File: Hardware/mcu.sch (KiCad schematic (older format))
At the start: 0 parts

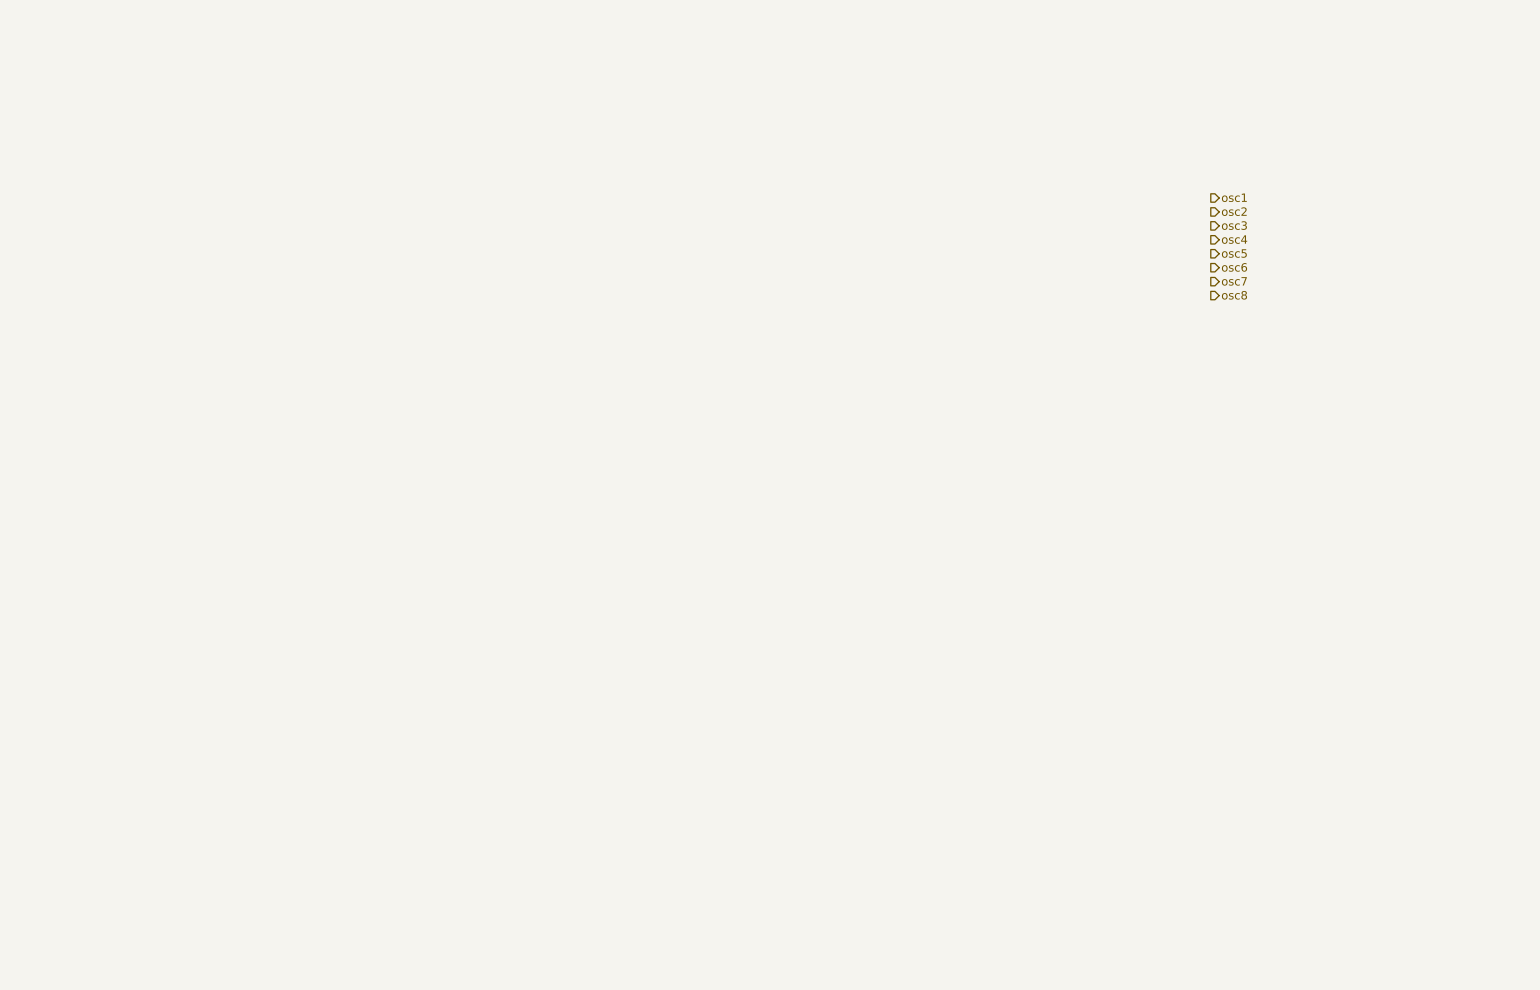
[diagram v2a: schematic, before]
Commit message: add all potentiometers for freq and pulse width
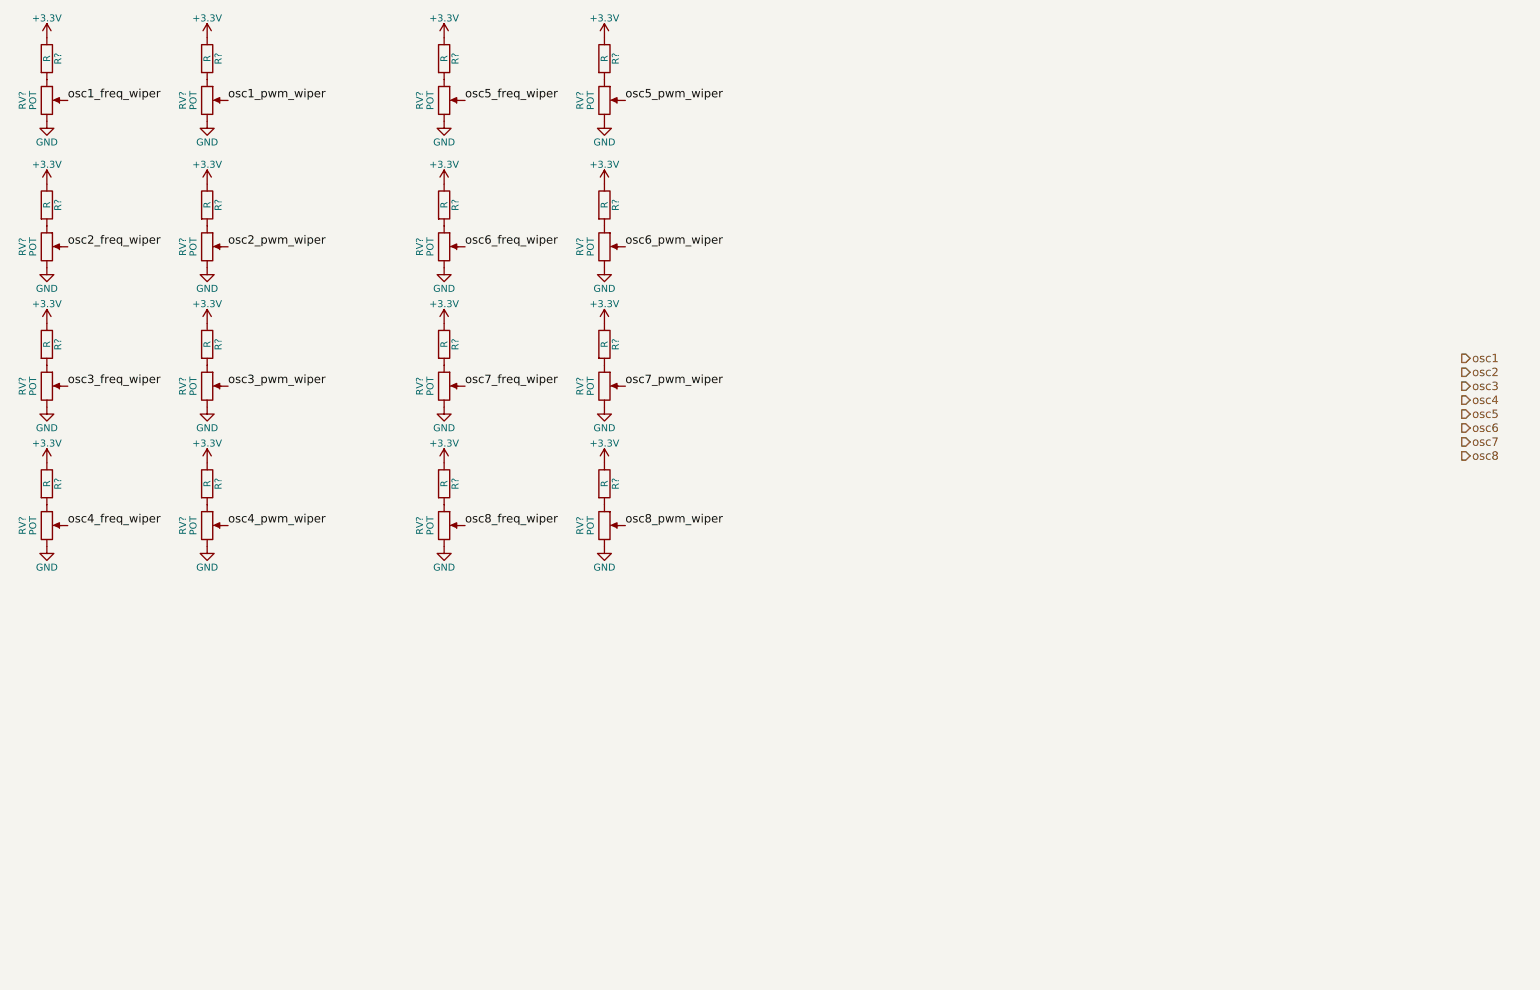
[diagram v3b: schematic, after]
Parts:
- added R? (x16): R, symbol R
- added RV? (x16): POT, symbol POT
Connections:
- new net: R?.2, RV?.1 (x16)
- new net +3V3: R?.1, R?.1, R?.1, R?.1, R?.1, R?.1, R?.1, R?.1, R?.1, R?.1, R?.1, R?.1, R?.1, R?.1, R?.1, R?.1
- new net GND: RV?.3, RV?.3, RV?.3, RV?.3, RV?.3, RV?.3, RV?.3, RV?.3, RV?.3, RV?.3, RV?.3, RV?.3, RV?.3, RV?.3, RV?.3, RV?.3
- new net osc1_freq_wiper: RV?.2
- new net osc1_pwm_wiper: RV?.2
- new net osc2_freq_wiper: RV?.2
- new net osc2_pwm_wiper: RV?.2
- new net osc3_freq_wiper: RV?.2
- new net osc3_pwm_wiper: RV?.2
- new net osc4_freq_wiper: RV?.2
- new net osc4_pwm_wiper: RV?.2
- new net osc5_freq_wiper: RV?.2
- new net osc5_pwm_wiper: RV?.2
- new net osc6_freq_wiper: RV?.2
- new net osc6_pwm_wiper: RV?.2
- new net osc7_freq_wiper: RV?.2
- new net osc7_pwm_wiper: RV?.2
- new net osc8_freq_wiper: RV?.2
- new net osc8_pwm_wiper: RV?.2

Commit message: add mcu, crystal, and programming header to schematic
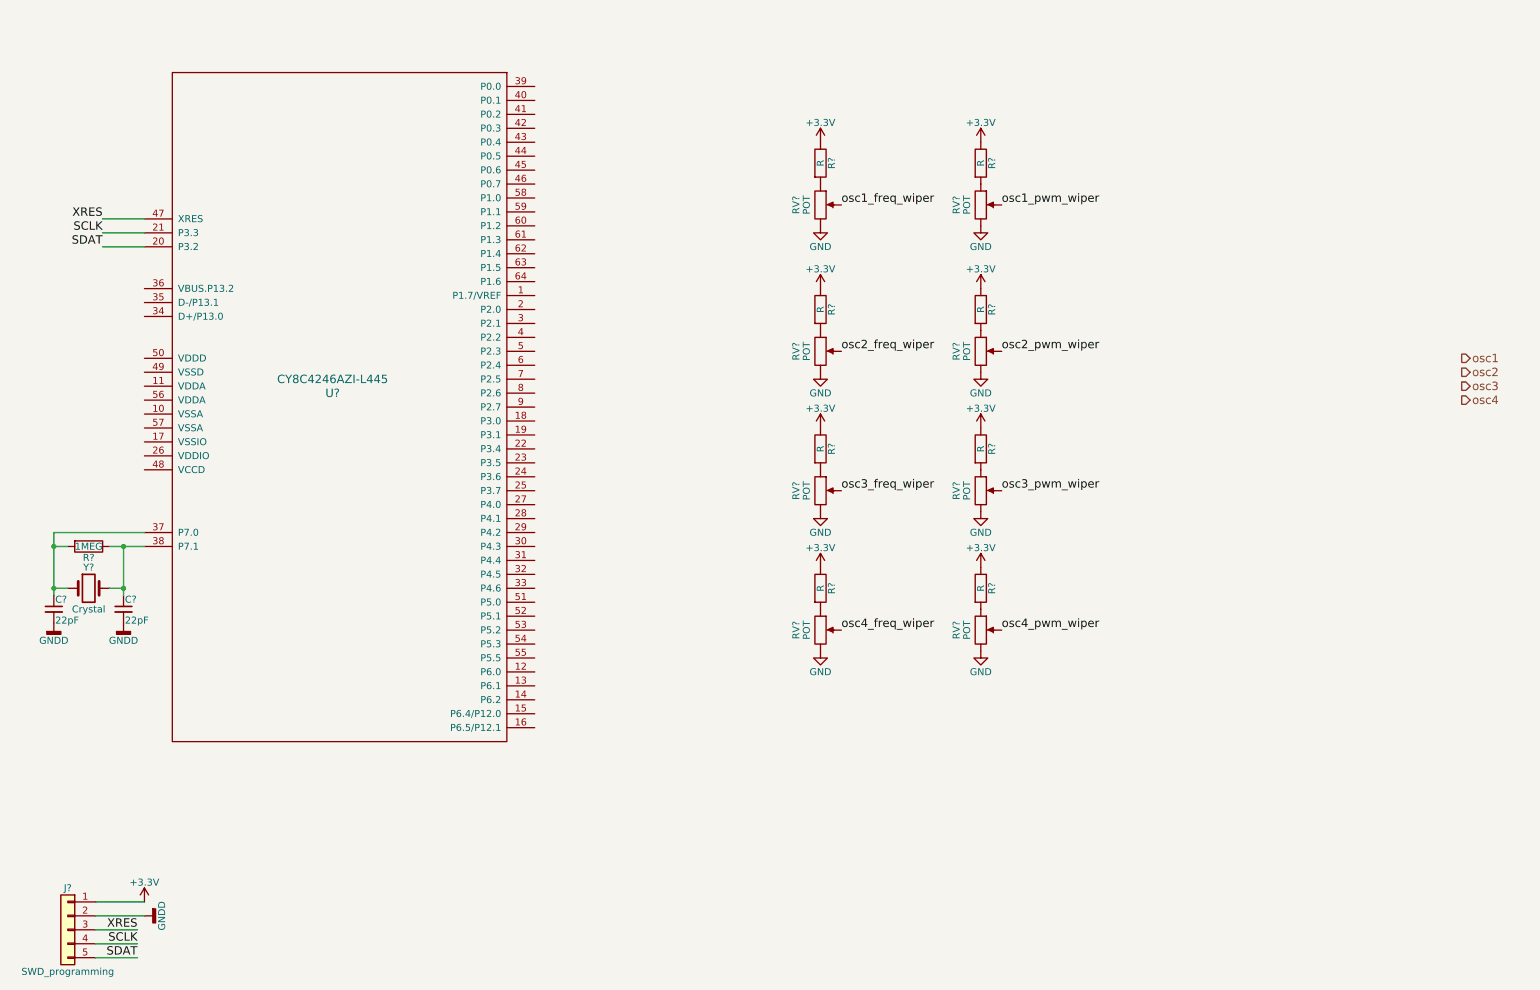
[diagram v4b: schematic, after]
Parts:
- removed R? (x8): R, symbol R
- removed RV? (x8): POT, symbol POT
- added C? (x2): 22pF, symbol C_Small
- added J?: SWD_programming, symbol Conn_01x05
- added R?: 1MEG, symbol R
- added U?: CY8C4246AZI-L445, symbol CY8C4246AZI-L445
- added Y?: Crystal, symbol Crystal
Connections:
- net +3V3: now also J?.1 (Pin_1)
- new net: C?.1, R?.2, U?.37 (P7.0), Y?.1
- new net: C?.1, R?.1, U?.38 (P7.1), Y?.2
- new net GNDD: C?.2, C?.2, J?.2 (Pin_2)
- new net SCLK: J?.4 (Pin_4), U?.21 (P3.3)
- new net SDAT: J?.5 (Pin_5), U?.20 (P3.2)
- new net XRES: J?.3 (Pin_3), U?.47 (XRES)
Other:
- moved on the sheet: R?, RV?

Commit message: connect frequency potentiometers to mcu
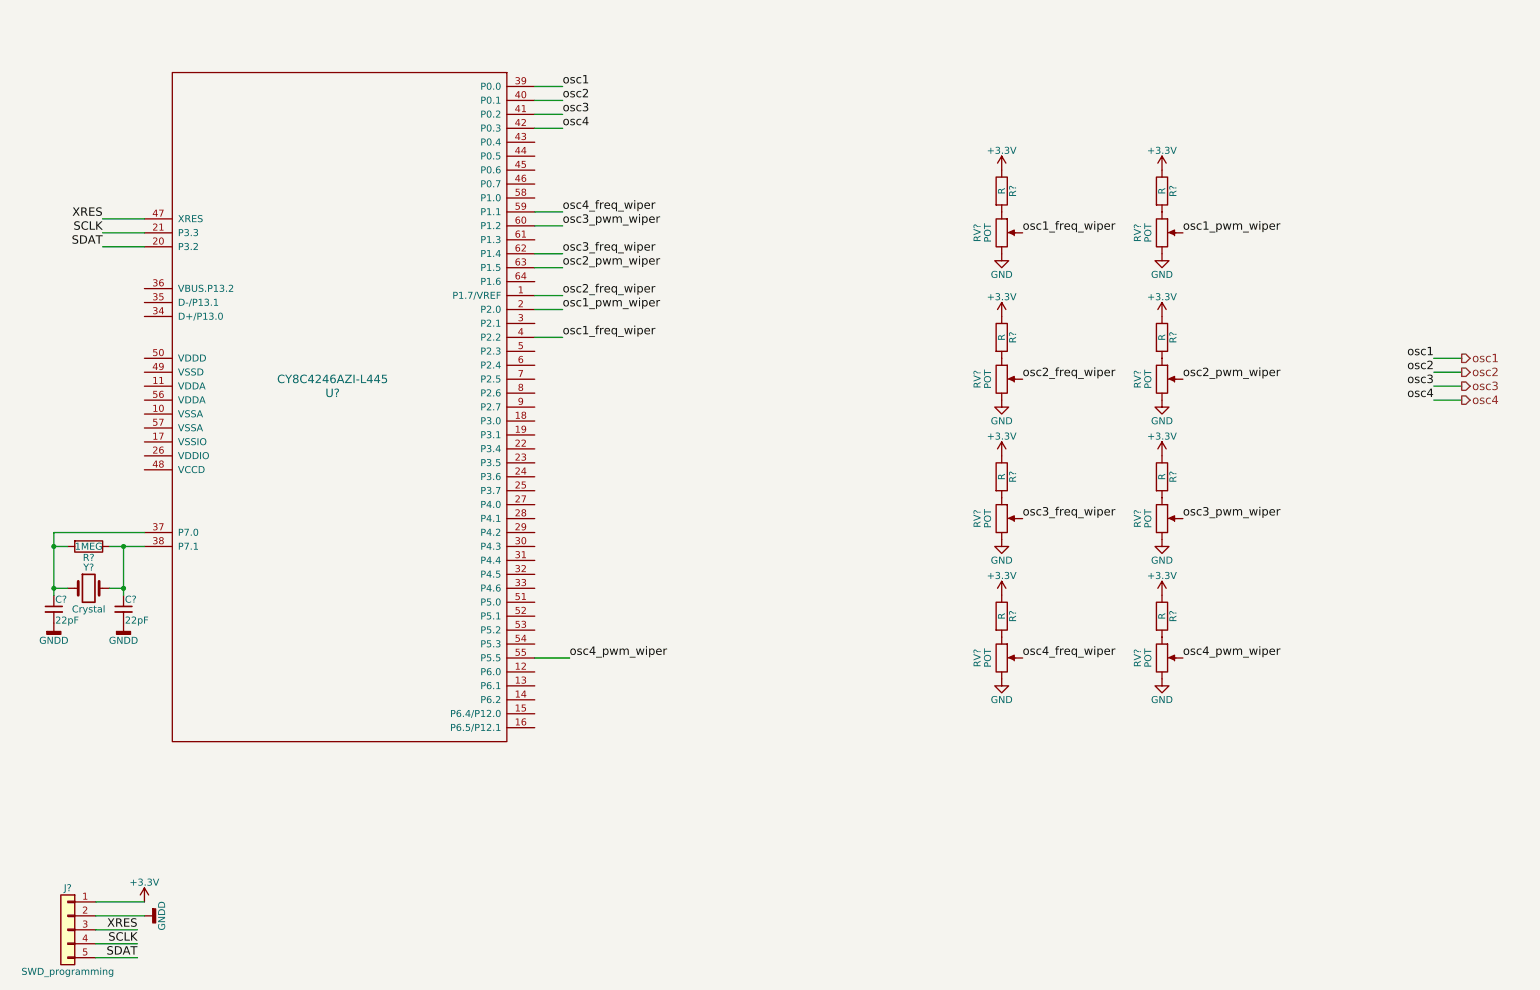
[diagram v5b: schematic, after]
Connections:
- net osc1: now also U?.39 (P0.0)
- net osc1_freq_wiper: now also U?.4 (P2.2)
- net osc1_pwm_wiper: now also U?.2 (P2.0)
- net osc2: now also U?.40 (P0.1)
- net osc2_freq_wiper: now also U?.1 (P1.7/VREF)
- net osc2_pwm_wiper: now also U?.63 (P1.5)
- net osc3: now also U?.41 (P0.2)
- net osc3_freq_wiper: now also U?.62 (P1.4)
- net osc3_pwm_wiper: now also U?.60 (P1.2)
- net osc4: now also U?.42 (P0.3)
- net osc4_freq_wiper: now also U?.59 (P1.1)
- net osc4_pwm_wiper: now also U?.55 (P5.5)
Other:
- moved on the sheet: R?, RV?

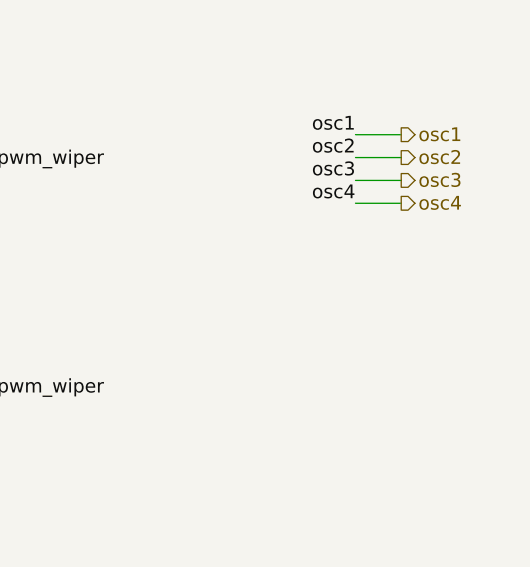
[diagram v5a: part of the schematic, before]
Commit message: complete wiring of top level schematic hierarchical pages
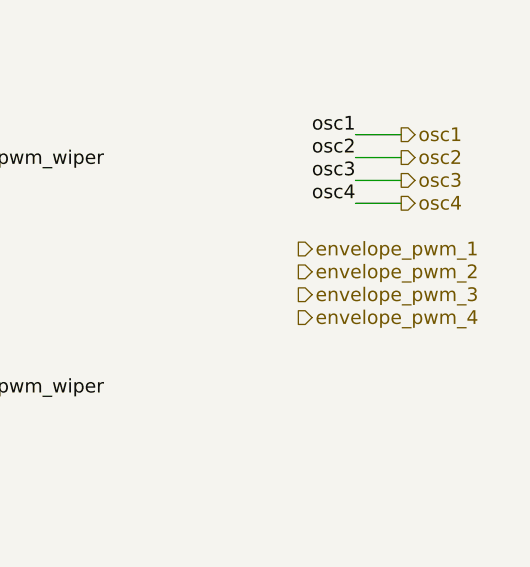
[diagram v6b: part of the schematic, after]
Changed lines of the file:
@@
 Wire Wire Line
 	10650 3350 10850 3350
+Text HLabel 10400 3550 2    60   Output ~ 0
+envelope_pwm_1
+Text HLabel 10400 3650 2    60   Output ~ 0
+envelope_pwm_2
+Text HLabel 10400 3750 2    60   Output ~ 0
+envelope_pwm_3
+Text HLabel 10400 3850 2    60   Output ~ 0
+envelope_pwm_4
 $EndSCHEMATC

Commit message: add power jack, 3.3V regulator, VREF divider
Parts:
- gave numbers to parts that had none: 22
